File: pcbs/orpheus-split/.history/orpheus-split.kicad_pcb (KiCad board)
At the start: 2 copper layers, 43 parts, among them SW1 SW_Push, SW10 SW_Push, SW11 SW_Push, SW12 SW_Push, SW13 SW_Push, SW14 SW_Push, SW15 SW_Push, SW16 SW_Push, SW17 SW_Push, SW18 SW_Push, SW19 SW_Push, SW2 SW_Push, SW20 SW_Push, SW21 SW_Push, SW3 SW_Push, SW4 SW_Push, SW5 SW_Push, SW6 SW_Push, SW7 SW_Push, SW8 SW_Push, SW9 SW_Push

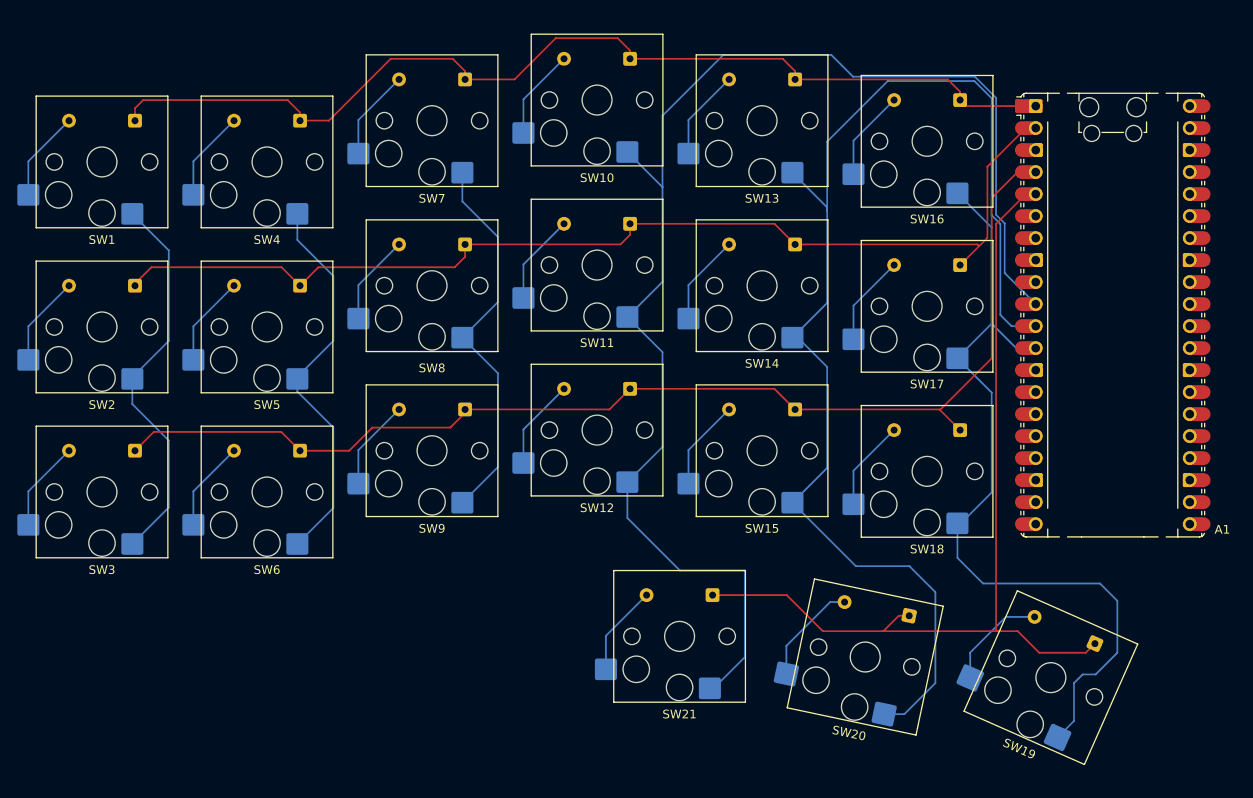
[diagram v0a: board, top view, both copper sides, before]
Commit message: finished the left pcb
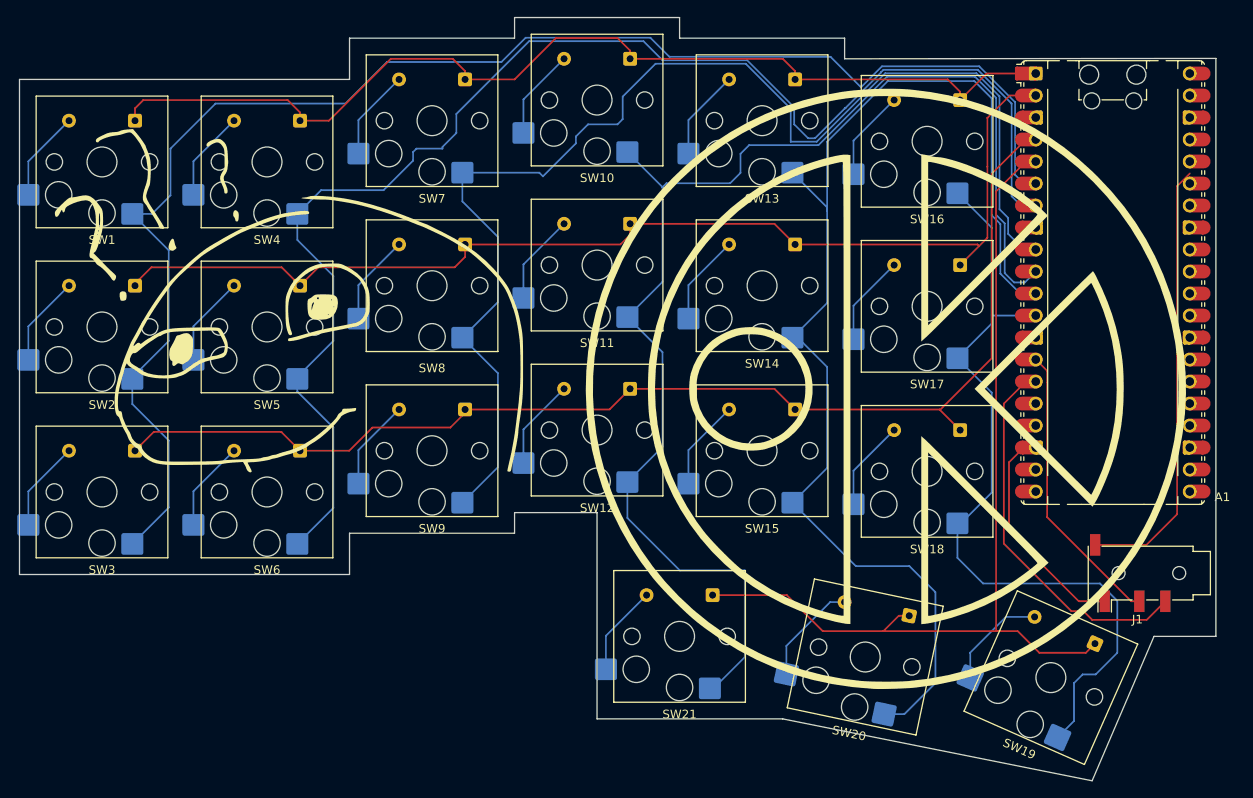
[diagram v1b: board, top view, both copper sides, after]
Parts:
- added G***: LOGO, LOGO, F.Cu at (154.8, 59.5)
- added G***: LOGO, LOGO, F.Cu at (85.7, 50.0)
- added J1: AudioJack4, Connector_Audio:Jack_3.5mm_PJ320D_Horizontal, F.Cu at (183.9, 80.8)
- moved A1 3.76 mm to (181.0, 47.3)
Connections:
- A1 pad 14: unconnected-(A1-GPIO10-Pad14) -> Net-(A1-GPIO10)
- A1 pad 15: unconnected-(A1-GPIO11-Pad15) -> Net-(A1-GPIO11)
- A1 pad 36: unconnected-(A1-3V3-Pad36) -> Net-(A1-3V3)
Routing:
- net /Col 0: track 45.1 -> 174.9 mm
- net /Col 1: track 45.0 -> 162.5 mm
- net /Col 2: track 44.9 -> 145.0 mm
- net Net-(A1-3V3): track 0.00 -> 50.9 mm
- net Net-(A1-GPIO11): track 0.00 -> 44.1 mm
- net Net-(A1-GPIO10): track 0.00 -> 33.4 mm
- net Net-(A1-GND-Pad13): track 0.00 -> 26.2 mm
- net /Col 3: track 158.0 -> 151.8 mm
- net /Row 1: track 125.0 -> 129.9 mm
- net /Col 4: track 144.6 -> 140.2 mm
- net /Row 3: track 104.6 -> 108.3 mm
- net /Row 2: track 135.5 -> 138.7 mm
- net /Col 5: track 95.2 -> 94.0 mm
- net /Row 0: track 118.7 -> 119.7 mm
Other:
- board outline added: 138.1 x 88.1 mm
- board text added: "PLS DONT BREAK!! XD"
